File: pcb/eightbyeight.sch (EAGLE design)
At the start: 136 parts, among them CON1 USB_MICROSMT+THRUHULE, Q1 16MHz, SW1 SWITCH_SPDT, SW2 BRIGHTNESS, U1 MK20DN64VFM5, U10 FDG6316P, U11 FDG6316P, U12 FDG6316P, U2 ICN2026, U3 74138, U4 ICN2026, U5 MIC5219 3.3V, U6 ESP_WROOM_02, U8 MMA8653FC, U9 FDG6316P

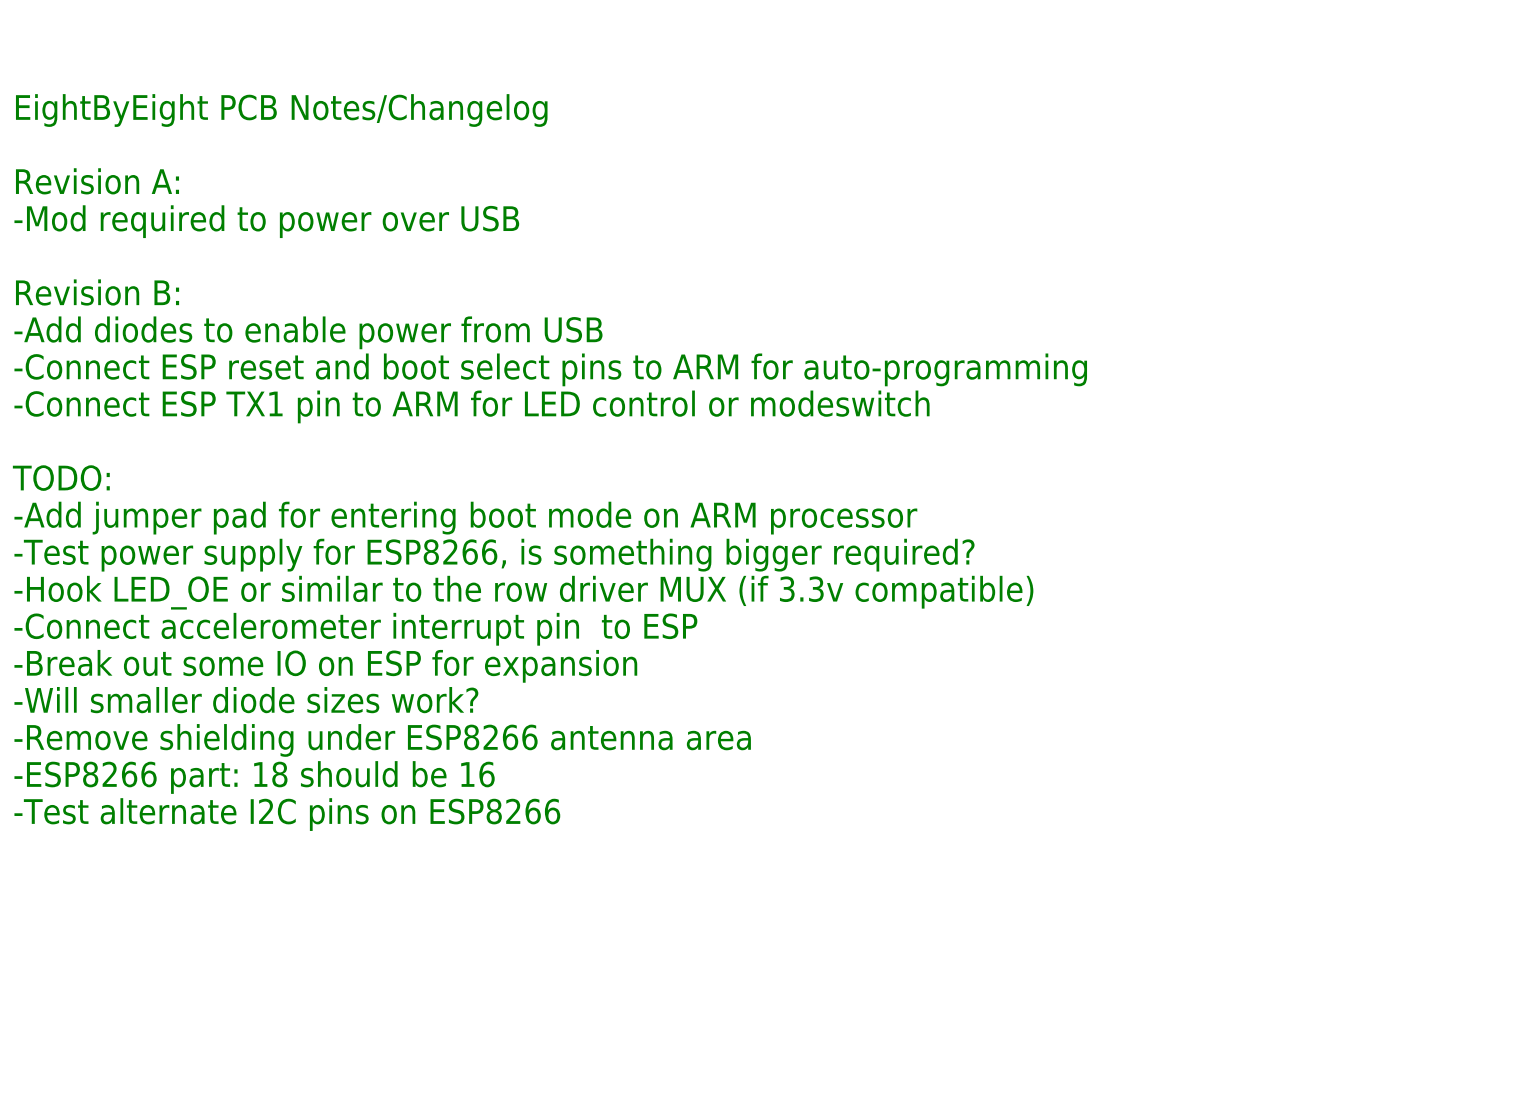
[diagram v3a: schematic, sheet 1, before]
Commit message: Finish routing accelerometer changes
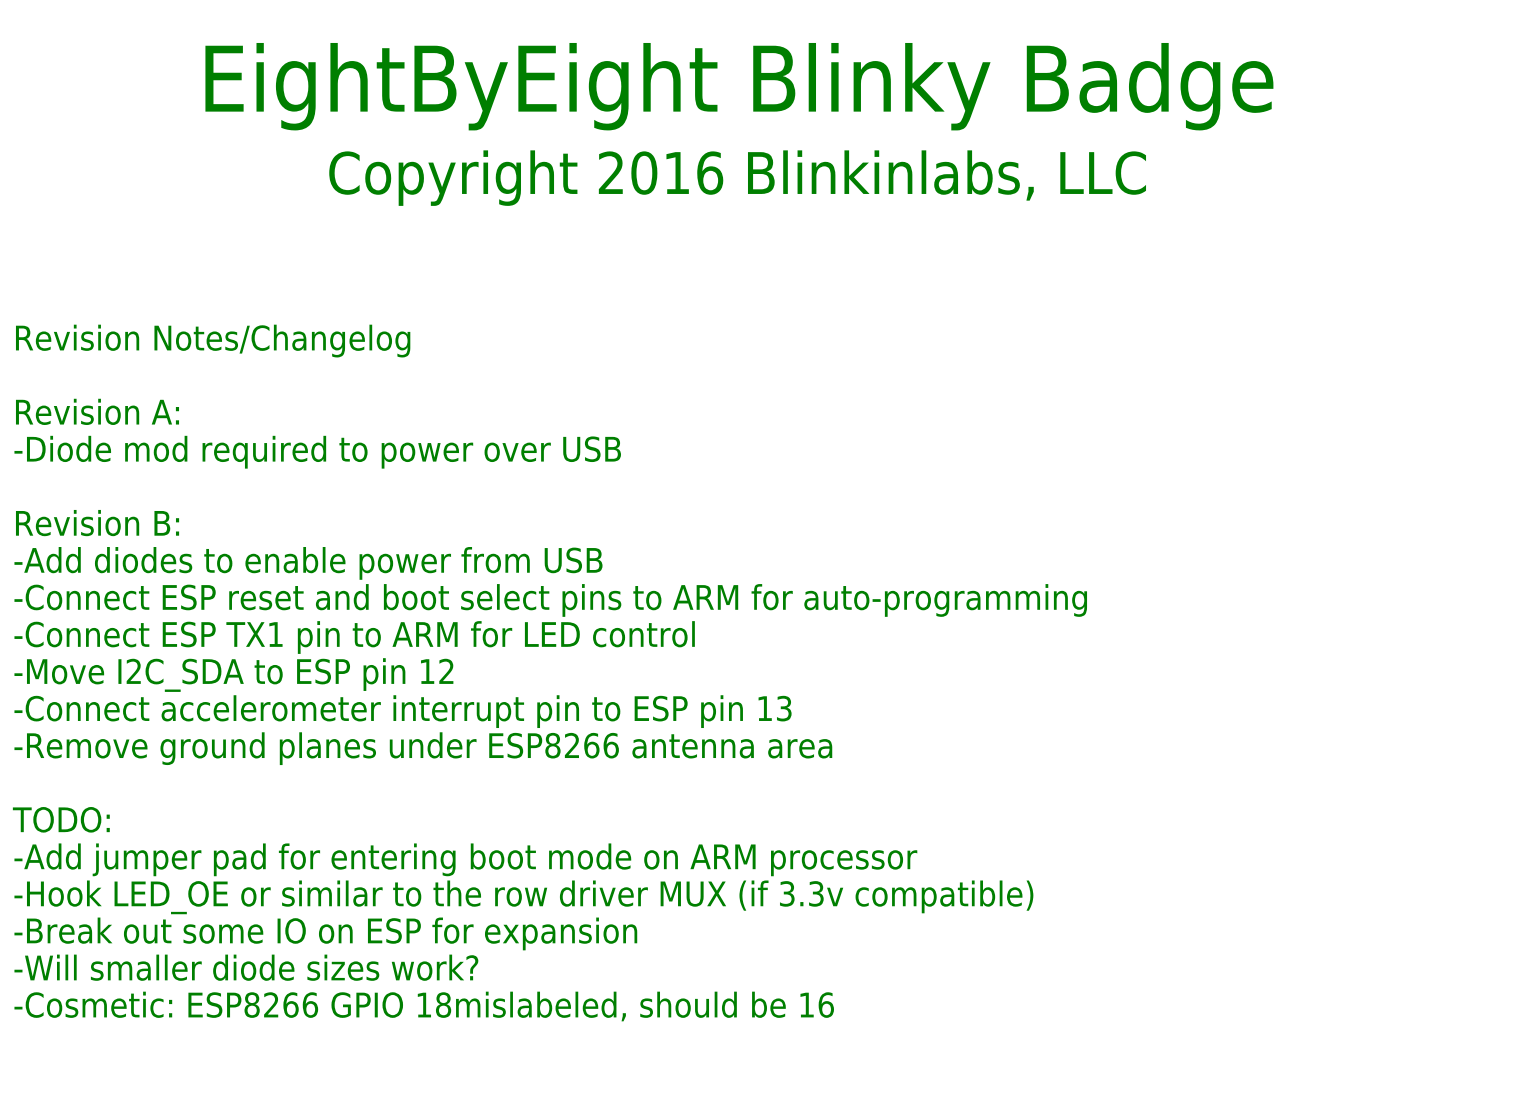
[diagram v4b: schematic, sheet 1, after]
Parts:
- removed TP2: PTR1B2,54, testpad:PTR1B2,54
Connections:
- removed net ESP_EXP_2: TP2.TP, U6.IO12
- new net I2C_SDA: R17.1, U6.IO12, U8.SDA
- net ARM_RX1: no longer R17.1, U8.SDA
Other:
- note added: "Copyright 2016 Blinkinlabs, LLC"
- note added: "EightByEight Blinky Badge"
- note added: "Pin assignments for USB/Serial conversion: ARM_RX and ARM_TX are UART0 ESP_RESET is virtually connected to RTS ESP_GPIO0 is virtually connected to DTR"
- note added: "Revision Notes/Changelog Revision A: -Diode mod required to power over USB Revision B: -Add diodes to enable power from USB -Connect ESP reset and boot select pins to ARM for auto-programming -Connect ESP TX1 pin to ARM for LED control -Move I2C_SDA to ESP pin 12 -Connect accelerometer interrupt pin to ESP pin 13 -Remove ground planes under ESP8266 antenna area TODO: -Add jumper pad for entering 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"
- note removed: "EightByEight PCB Notes/Changelog Revision A: -Mod required to power over USB Revision B: -Add diodes to enable power from USB -Connect ESP reset and boot select pins to ARM for auto-programming -Connect ESP TX1 pin to ARM for LED control or modeswitch TODO: -Add jumper pad for entering boot mode on ARM processor -Test power supply for ESP8266, is something bigger required? -Hook LED_OE or similar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"
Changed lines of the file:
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@@
 <part name="GND43" library="SparkFun-Aesthetics" deviceset="GND" device=""/>
 <part name="TP1" library="testpad" deviceset="PTR1" device="B2,54"/>
-<part name="TP2" library="testpad" deviceset="PTR1" device="B2,54"/>
 <part name="TP3" library="testpad" deviceset="PTR1" device="B2,54"/>
 <part name="ANALOG_IN" library="testpad" deviceset="PTR1" device="B2,54"/>
@@
 <sheet>
 <plain>
-<text x="17.78" y="360.68" size="3.81" layer="91" align="top-left">EightByEight PCB Notes/Changelog
+<text x="17.78" y="325.12" size="3.81" layer="91" align="top-left">Revision Notes/Changelog
 Revision A:
--Mod required to power over USB
+-Diode mod required to power over USB
 Revision B:
 -Add diodes to enable power from USB
 -Connect ESP reset and boot select pins to ARM for auto-programming
--Connect ESP TX1 pin to ARM for LED control or modeswitch
+-Connect ESP TX1 pin to ARM for LED control
+-Move I2C_SDA to ESP pin 12
+-Connect accelerometer interrupt pin to ESP pin 13
+-Remove ground planes under ESP8266 antenna area
 TODO:
 -Add jumper pad for entering boot mode on ARM processor
--Test power supply for ESP8266, is something bigger required?
 -Hook LED_OE or similar to the row driver MUX (if 3.3v compatible)
--Connect accelerometer interrupt pin  to ESP
 -Break out some IO on ESP for expansion
 -Will smaller diode sizes work?
--Remove shielding under ESP8266 antenna area
--ESP8266 part: 18 should be 16
--Test alternate I2C pins on ESP8266</text>
+-Cosmetic: ESP8266 GPIO 18mislabeled, should be 16</text>
+<text x="129.54" y="358.14" size="10.16" layer="91" align="bottom-center">EightByEight Blinky Badge</text>
+<text x="129.54" y="345.44" size="6.4516" layer="91" align="bottom-center">Copyright 2016 Blinkinlabs, LLC</text>
 </plain>
 <instances>
@@
 <wire x1="7.62" y1="10.16" x2="121.92" y2="10.16" width="0.4064" layer="94"/>
 <wire x1="121.92" y1="10.16" x2="121.92" y2="86.36" width="0.4064" layer="94"/>
+<text x="76.2" y="116.84" size="1.778" layer="91">Pin assignments for USB/Serial conversion:
+ARM_RX and ARM_TX are UART0
+ESP_RESET is virtually connected to RTS
+ESP_GPIO0 is virtually connected to DTR</text>
 </plain>
 <instances>
@@
 </instance>
 <instance part="TP1" gate="G$1" x="287.02" y="215.9" rot="R90"/>
-<instance part="TP2" gate="G$1" x="287.02" y="220.98" rot="R90"/>
 <instance part="TP3" gate="G$1" x="287.02" y="226.06" rot="R90"/>
 <instance part="ANALOG_IN" gate="G$1" x="287.02" y="210.82" rot="R90"/>
@@
 </segment>
 <segment>
-<pinref part="R17" gate="G$1" pin="1"/>
-<wire x1="20.32" y1="129.54" x2="20.32" y2="109.22" width="0.1524" layer="91"/>
-<label x="20.32" y="109.22" size="1.778" layer="95" rot="R90"/>
-</segment>
-<segment>
-<pinref part="U8" gate="G$1" pin="SDA"/>
-<wire x1="236.22" y1="139.7" x2="254" y2="139.7" width="0.1524" layer="91"/>
-<label x="241.3" y="139.7" size="1.778" layer="95"/>
-</segment>
-<segment>
 <wire x1="180.34" y1="200.66" x2="162.56" y2="200.66" width="0.1524" layer="91"/>
 <pinref part="R12" gate="G$1" pin="1"/>
@@
 </segment>
 </net>
-<net name="ESP_EXP_2" class="0">
+<net name="ESP_EXP_3" class="0">
+<segment>
+<pinref part="U6" gate="G$1" pin="IO18"/>
+<wire x1="86.36" y1="200.66" x2="104.14" y2="200.66" width="0.1524" layer="91"/>
+<label x="91.44" y="200.66" size="1.778" layer="95"/>
+</segment>
+<segment>
+<pinref part="TP1" gate="G$1" pin="TP"/>
+<wire x1="284.48" y1="215.9" x2="264.16" y2="215.9" width="0.1524" layer="91"/>
+<label x="266.7" y="215.9" size="1.778" layer="95"/>
+</segment>
+</net>
+<net name="ESP_TOUT" class="0">
+<segment>
+<pinref part="ANALOG_IN" gate="G$1" pin="TP"/>
+<wire x1="284.48" y1="210.82" x2="264.16" y2="210.82" width="0.1524" layer="91"/>
+<label x="266.7" y="210.82" size="1.778" layer="95"/>
+</segment>
+<segment>
+<pinref part="U6" gate="G$1" pin="TOUT"/>
+<wire x1="53.34" y1="205.74" x2="25.4" y2="205.74" width="0.1524" layer="91"/>
+<label x="27.94" y="205.74" size="1.778" layer="95"/>
+</segment>
+</net>
+<net name="I2C_SDA" class="0">
 <segment>
 <pinref part="U6" gate="G$1" pin="IO12"/>
@@
 </segment>
 <segment>
-<pinref part="TP2" gate="G$1" pin="TP"/>
-<wire x1="264.16" y1="220.98" x2="284.48" y2="220.98" width="0.1524" layer="91"/>
-<label x="266.7" y="220.98" size="1.778" layer="95"/>
-</segment>
-</net>
-<net name="ESP_EXP_3" class="0">
-<segment>
-<pinref part="U6" gate="G$1" pin="IO18"/>
-<wire x1="86.36" y1="200.66" x2="104.14" y2="200.66" width="0.1524" layer="91"/>
-<label x="91.44" y="200.66" size="1.778" layer="95"/>
-</segment>
-<segment>
-<pinref part="TP1" gate="G$1" pin="TP"/>
-<wire x1="284.48" y1="215.9" x2="264.16" y2="215.9" width="0.1524" layer="91"/>
-<label x="266.7" y="215.9" size="1.778" layer="95"/>
-</segment>
-</net>
-<net name="ESP_TOUT" class="0">
-<segment>
-<pinref part="ANALOG_IN" gate="G$1" pin="TP"/>
-<wire x1="284.48" y1="210.82" x2="264.16" y2="210.82" width="0.1524" layer="91"/>
-<label x="266.7" y="210.82" size="1.778" layer="95"/>
-</segment>
-<segment>
-<pinref part="U6" gate="G$1" pin="TOUT"/>
-<wire x1="53.34" y1="205.74" x2="25.4" y2="205.74" width="0.1524" layer="91"/>
-<label x="27.94" y="205.74" size="1.778" layer="95"/>
-</segment>
-</net>
+<pinref part="R17" gate="G$1" pin="1"/>
+<wire x1="20.32" y1="129.54" x2="20.32" y2="109.22" width="0.1524" layer="91"/>
+<label x="20.32" y="109.22" size="1.778" layer="95" rot="R90"/>
+</segment>
+<segment>
+<pinref part="U8" gate="G$1" pin="SDA"/>
+<wire x1="236.22" y1="139.7" x2="254" y2="139.7" width="0.1524" layer="91"/>
+<label x="241.3" y="139.7" size="1.778" layer="95"/>
+</segment>
+</net>
